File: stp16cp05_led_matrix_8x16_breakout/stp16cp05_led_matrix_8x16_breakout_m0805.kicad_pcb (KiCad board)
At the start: 2 copper layers, 101 x 83 mm, 174 parts, among them J1 (Input/Output) LED Matrix 2.5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, J2 (Input/Output) LED Matrix (SM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, Q1 DMP3125L-7, Q2 DMP3125L-7, Q3 DMP3125L-7, Q4 DMP3125L-7, Q5 DMP3125L-7, Q6 DMP3125L-7, Q7 DMP3125L-7, Q8 DMP3125L-7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

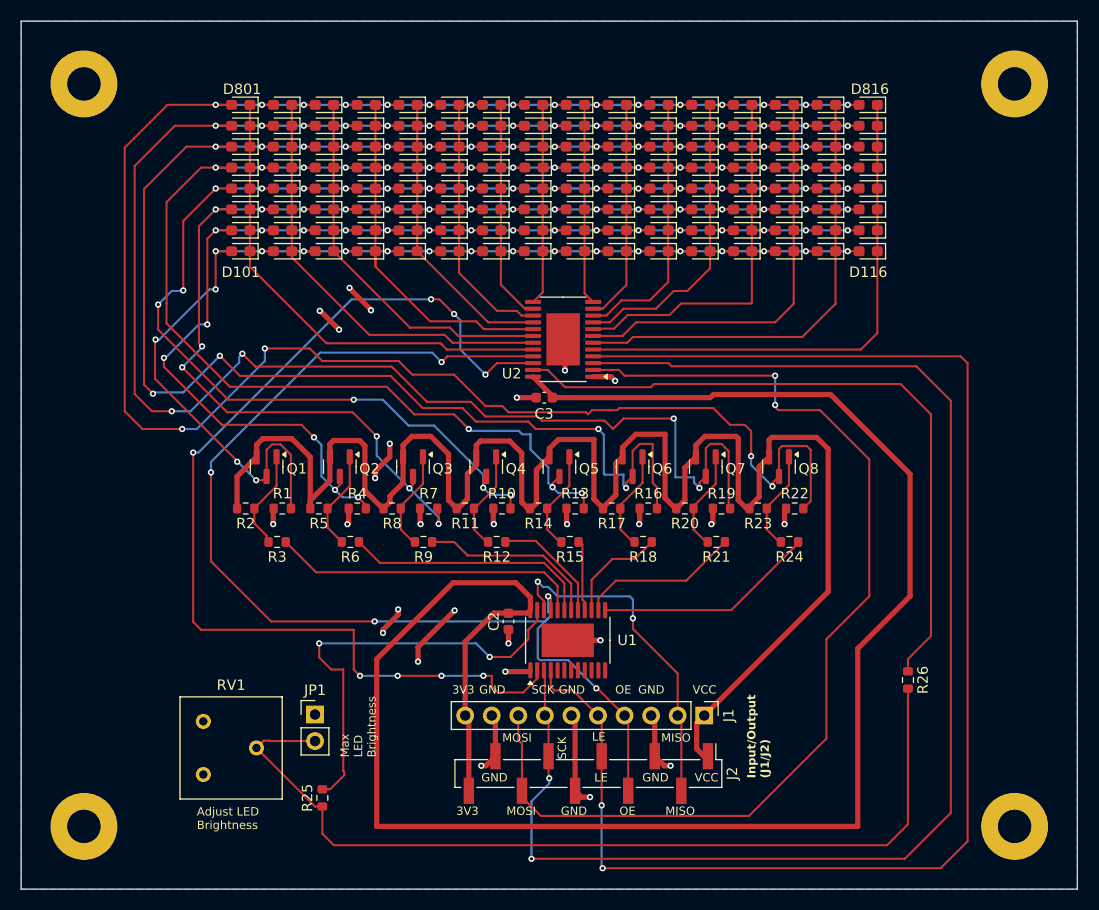
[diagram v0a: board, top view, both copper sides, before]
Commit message: Update pcb (flip led rows)
- Flipped LED rows to stop the crossing tracks between layers
- Updated gerbers and images too
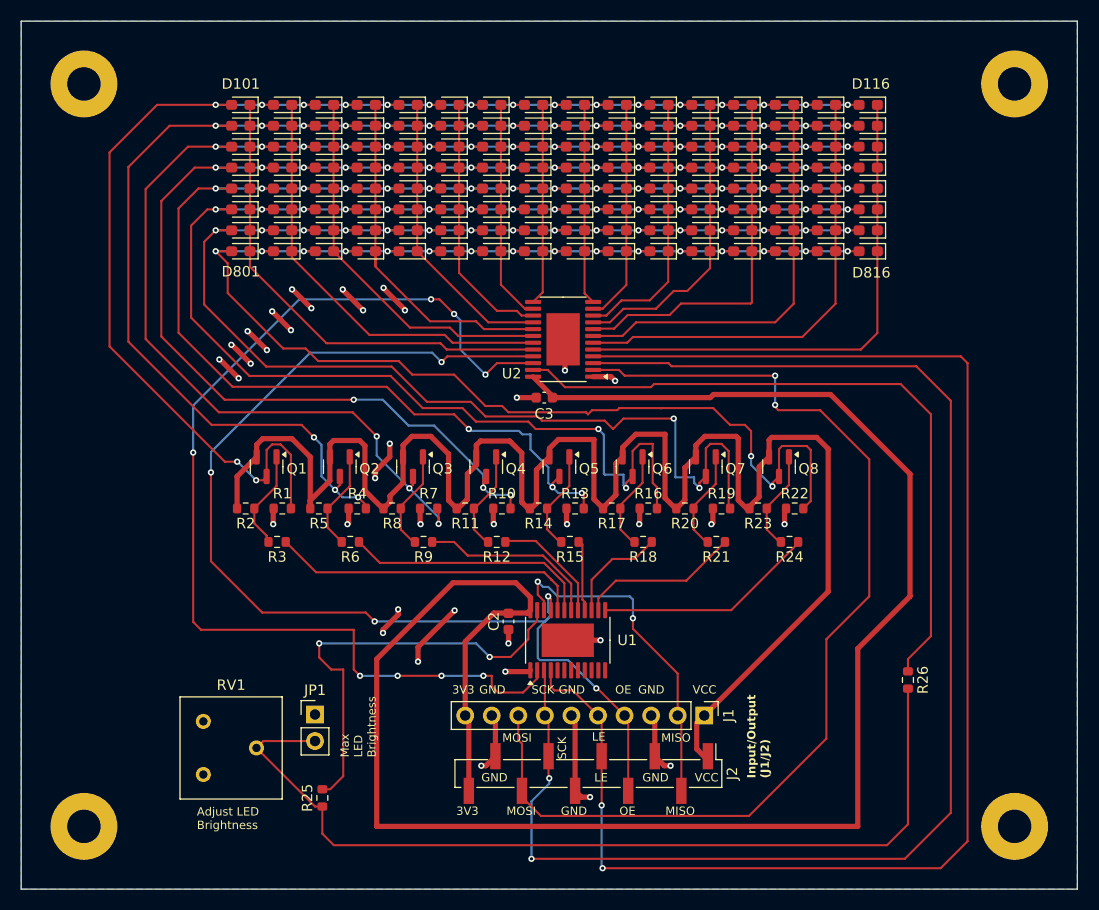
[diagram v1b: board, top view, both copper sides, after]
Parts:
- moved D101 14.0 mm to (160.0, 50.0)
- moved D102 14.0 mm to (164.0, 50.0)
- moved D103 14.0 mm to (168.0, 50.0)
- moved D104 14.0 mm to (172.0, 50.0)
- moved D105 14.0 mm to (176.0, 50.0)
- moved D106 14.0 mm to (180.0, 50.0)
- moved D107 14.0 mm to (184.0, 50.0)
- moved D108 14.0 mm to (188.0, 50.0)
- moved D109 14.0 mm to (192.0, 50.0)
- moved D110 14.0 mm to (196.0, 50.0)
- moved D111 14.0 mm to (200.0, 50.0)
- moved D112 14.0 mm to (204.0, 50.0)
- moved D113 14.0 mm to (208.0, 50.0)
- moved D114 14.0 mm to (212.0, 50.0)
- moved D115 14.0 mm to (216.0, 50.0)
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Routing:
- net /ROW8: track 201.4 -> 158.0 mm, vias 20 -> 18
- net /ROW7: track 188.8 -> 157.2 mm, vias 20 -> 18
- net /ROW1: track 119.0 -> 140.0 mm, vias 20 -> 18
- net /ROW6: track 173.9 -> 153.6 mm, vias 20 -> 18
- net /ROW2: track 122.4 -> 137.8 mm, vias 21 -> 19
- net GND: track 65.6 -> 78.5 mm, vias 27 -> 37
- net /ROW3: track 130.0 -> 140.6 mm, vias 21 -> 19
- net /ROW5: track 146.8 -> 143.8 mm
- net Net-(U1-SDI): track 99.7 -> 102.3 mm
- net /ROW4: track 138.2 -> 140.7 mm, vias 21 -> 19
- net /OE: track 106.3 -> 106.9 mm

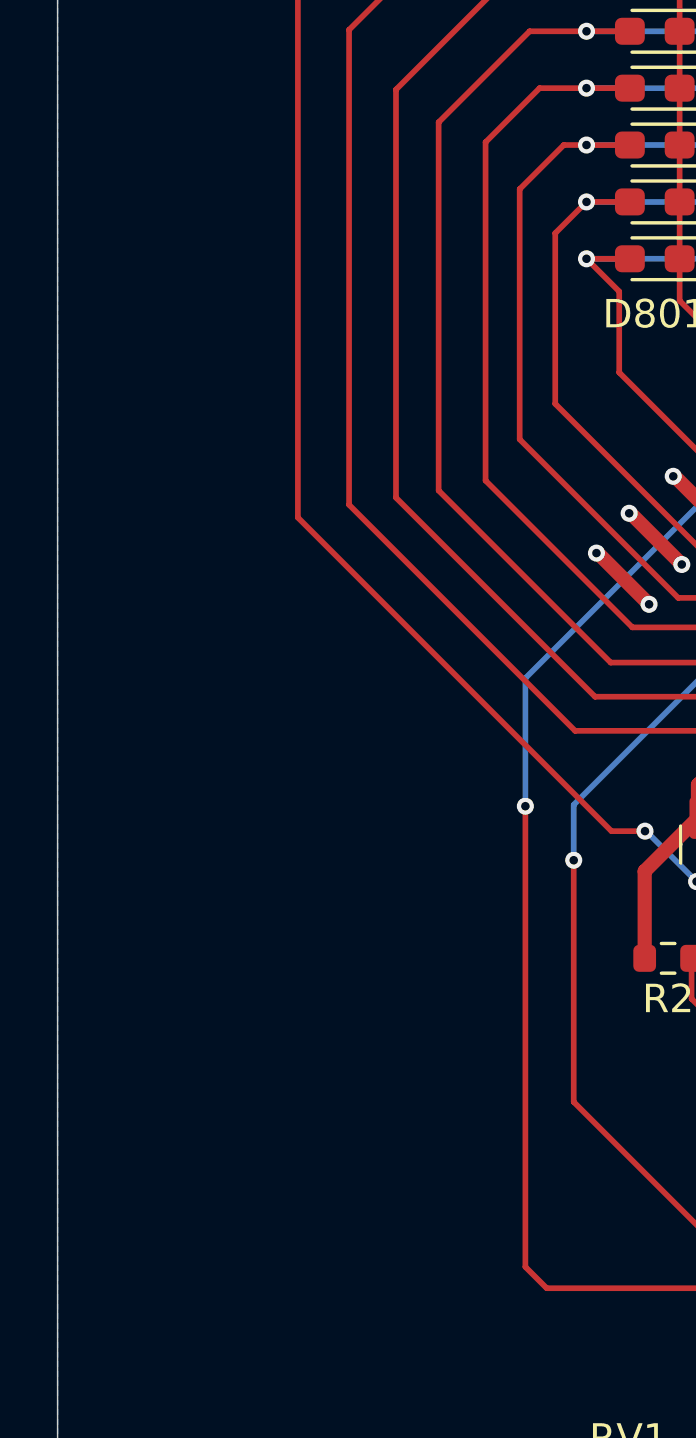
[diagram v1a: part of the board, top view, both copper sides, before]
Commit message: Add pcb revision number and text (to front silkscreen)
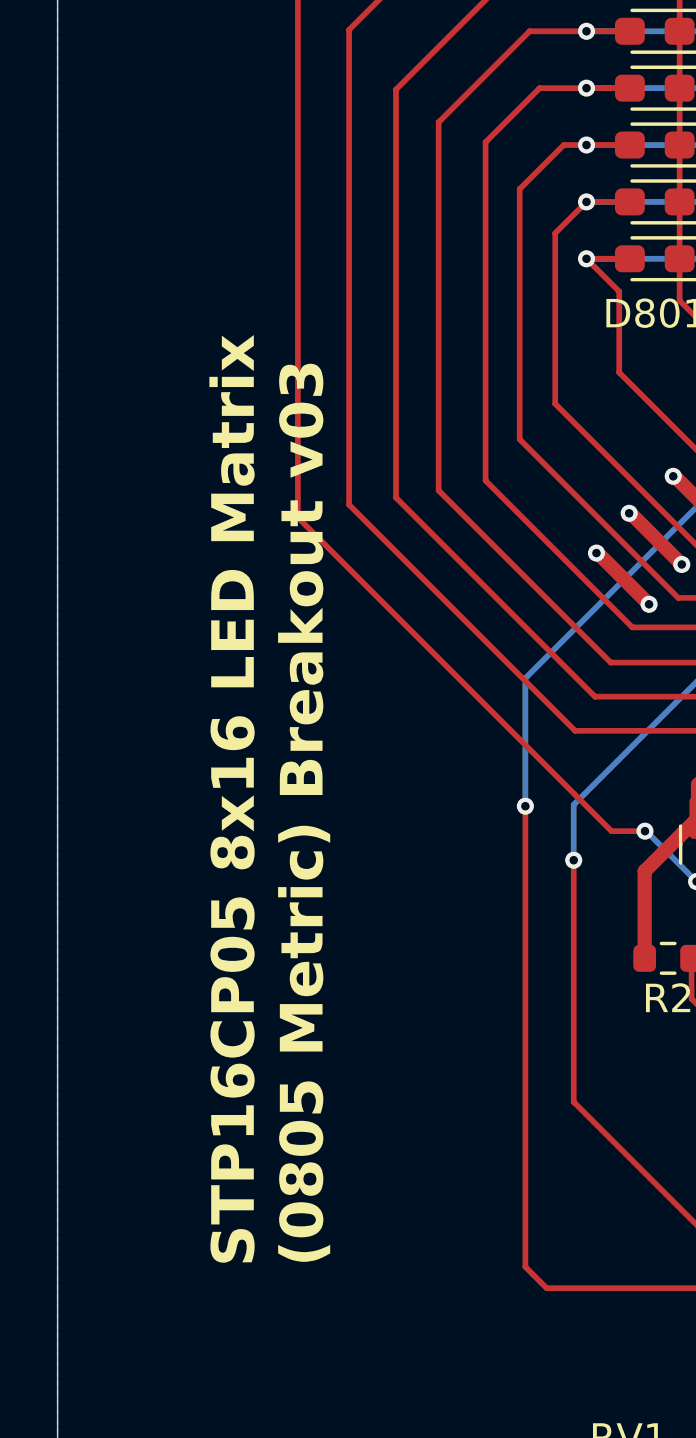
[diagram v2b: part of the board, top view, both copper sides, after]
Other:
- board text added: "STP16CP05 8x16 LED Matrix (0805 Metric) Breakout v03"
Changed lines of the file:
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@@
+		)
+	)
+	(gr_text "STP16CP05 8x16 LED Matrix\n(0805 Metric) Breakout v03"
+		(at 148.5 99.45 90)
+		(layer "F.SilkS")
+		(effects
+			(font
+				(size 1.5 1.5)
+				(thickness 0.3)
+				(bold yes)
+			)
+			(justify left bottom)
 		)
 	)
